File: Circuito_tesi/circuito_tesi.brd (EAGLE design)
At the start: 19 parts, among them IC1 317T, IC2 317T, IC3 317T, U1 NRF52832, U2 BME688

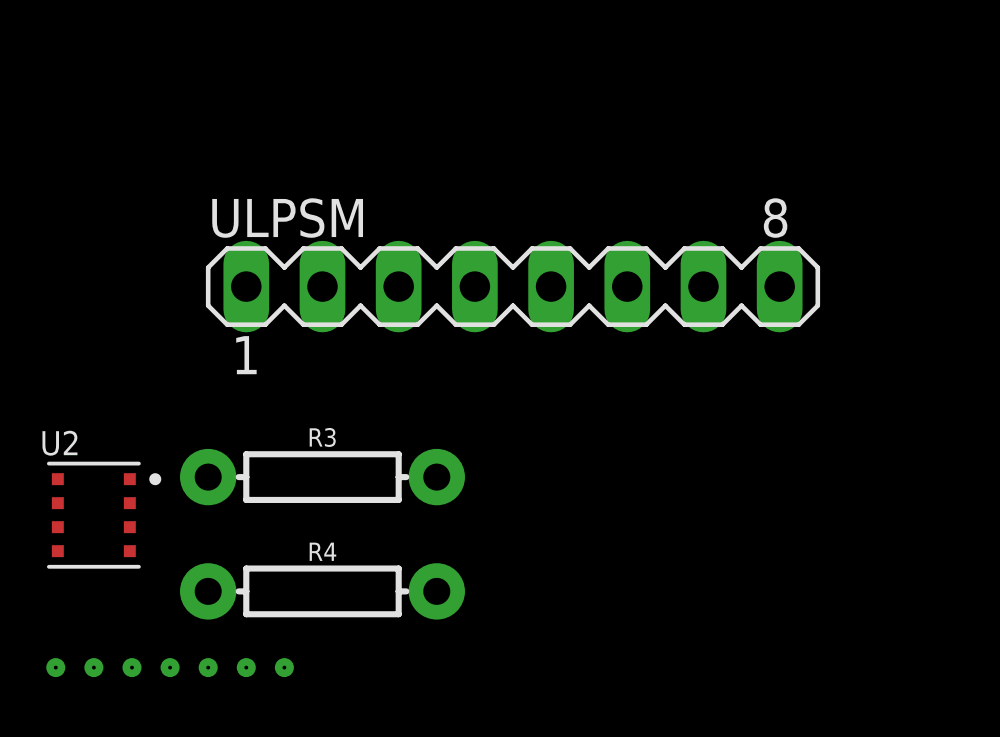
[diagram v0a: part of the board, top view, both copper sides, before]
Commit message: Attivato saadc
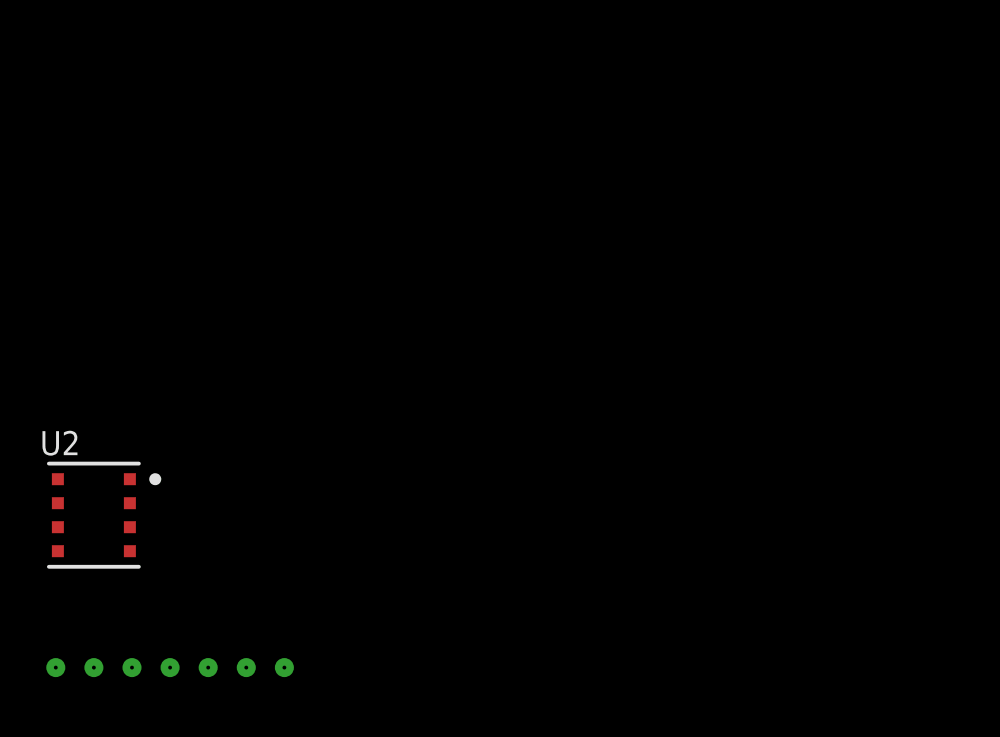
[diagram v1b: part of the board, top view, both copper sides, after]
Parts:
- removed R3, R4: 10k, SparkFun-Resistors:AXIAL-0.3
- removed ULPSM: (no value), con-lstb:MA08-1
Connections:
- removed net N$10: ULPSM.1
- removed net N$6: R3.P$2, R4.P$1, ULPSM.2
- net 3.3: no longer R3.P$1, R4.P$2, ULPSM.6, ULPSM.8
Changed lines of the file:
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@@
 <attribute name="VALUE" x="-93.98" y="-49.276" size="0.6096" layer="27" font="vector" ratio="20" align="top-center"/>
-</element>
-<element name="ULPSM" library="con-lstb" library_urn="urn:adsk.eagle:library:162" package="MA08-1" package3d_urn="urn:adsk.eagle:package:8343/1" value="" x="-87.63" y="-69.85" smashed="yes">
-<attribute name="MF" value="" x="-87.63" y="-69.85" size="1.778" layer="27" display="off"/>
-<attribute name="MPN" value="" x="-87.63" y="-69.85" size="1.778" layer="27" display="off"/>
-<attribute name="NAME" x="-97.79" y="-68.199" size="1.27" layer="25" ratio="10"/>
-<attribute name="OC_FARNELL" value="unknown" x="-87.63" y="-69.85" size="1.778" layer="27" display="off"/>
-<attribute name="OC_NEWARK" value="unknown" x="-87.63" y="-69.85" size="1.778" layer="27" display="off"/>
-<attribute name="POPULARITY" value="10" x="-87.63" y="-69.85" size="1.778" layer="27" display="off"/>
-<attribute name="VALUE" x="-88.9" y="-72.771" size="1.27" layer="27" ratio="10"/>
-</element>
-<element name="R3" library="SparkFun-Resistors" package="AXIAL-0.3" value="10k" x="-93.98" y="-76.2" smashed="yes">
-<attribute name="NAME" x="-93.98" y="-75.184" size="0.6096" layer="25" font="vector" ratio="20" align="bottom-center"/>
-<attribute name="PROD_ID" value="RES-08375" x="-93.98" y="-76.2" size="1.778" layer="27" display="off"/>
-<attribute name="VALUE" x="-93.98" y="-77.216" size="0.6096" layer="27" font="vector" ratio="20" align="top-center"/>
-</element>
-<element name="R4" library="SparkFun-Resistors" package="AXIAL-0.3" value="10k" x="-93.98" y="-80.01" smashed="yes">
-<attribute name="NAME" x="-93.98" y="-78.994" size="0.6096" layer="25" font="vector" ratio="20" align="bottom-center"/>
-<attribute name="PROD_ID" value="RES-08375" x="-93.98" y="-80.01" size="1.778" layer="27" display="off"/>
-<attribute name="VALUE" x="-93.98" y="-81.026" size="0.6096" layer="27" font="vector" ratio="20" align="top-center"/>
 </element>
 <element name="U2" library="BME688" package="IC_BME688" value="BME688" x="-101.6" y="-77.47" smashed="yes">
@@
 <contactref element="B1" pad="GND1"/>
 <contactref element="B1" pad="GND2"/>
-<contactref element="R4" pad="P$2"/>
-<contactref element="ULPSM" pad="6"/>
-<contactref element="ULPSM" pad="8"/>
-<contactref element="R3" pad="P$1"/>
 <contactref element="IC2" pad="2"/>
 <contactref element="C2" pad="1"/>
@@
 <wire x1="-102.8" y1="-76.27" x2="-102.8" y2="-77.87" width="0" layer="19" extent="1-1"/>
 <wire x1="-100.4" y1="-77.07" x2="-102.8" y2="-77.87" width="0" layer="19" extent="1-1"/>
-<wire x1="-97.79" y1="-76.2" x2="-100.4" y2="-77.07" width="0" layer="19" extent="1-1"/>
-<wire x1="-95.25" y1="-82.55" x2="-97.79" y2="-76.2" width="0" layer="19" extent="1-1"/>
-<wire x1="-90.17" y1="-80.01" x2="-95.25" y2="-82.55" width="0" layer="19" extent="1-1"/>
-<wire x1="-83.82" y1="-69.85" x2="-90.17" y2="-80.01" width="0" layer="19" extent="1-1"/>
-<wire x1="-78.74" y1="-69.85" x2="-83.82" y2="-69.85" width="0" layer="19" extent="1-1"/>
-<wire x1="-90.17" y1="-48.26" x2="-83.82" y2="-69.85" width="0" layer="19" extent="1-1"/>
+<wire x1="-95.25" y1="-82.55" x2="-100.4" y2="-77.07" width="0" layer="19" extent="1-1"/>
+<wire x1="-90.17" y1="-48.26" x2="-100.4" y2="-77.07" width="0" layer="19" extent="1-1"/>
 <wire x1="-90.17" y1="-44.45" x2="-90.17" y2="-48.26" width="0" layer="19" extent="1-1"/>
 <wire x1="-95.67" y1="-33.02" x2="-90.17" y2="-44.45" width="0" layer="19" extent="1-1"/>
@@
 <wire x1="-15.11" y1="-10.48" x2="-81.28" y2="-8.89" width="0" layer="19" extent="1-1"/>
 </signal>
-<signal name="N$6">
-<contactref element="R3" pad="P$2"/>
-<contactref element="ULPSM" pad="2"/>
-<contactref element="R4" pad="P$1"/>
-<wire x1="-90.17" y1="-76.2" x2="-97.79" y2="-80.01" width="0" layer="19" extent="1-1"/>
-<wire x1="-93.98" y1="-69.85" x2="-90.17" y2="-76.2" width="0" layer="19" extent="1-1"/>
-</signal>
-<signal name="N$10">
-<contactref element="ULPSM" pad="1"/>
-</signal>
 <signal name="N$8">

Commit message: Aggiunta lettura MICS6814
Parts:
- removed C3: 0.1uF, SparkFun-Capacitors:0603
- removed C4: 22uF, SparkFun-Capacitors:0805
- removed IC3: 317T, linear:TO220H
- added U3: MICS-6814, MICS-6814:SENSOR_MICS-6814
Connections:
- removed net N$2: C4.1, IC3.2
- net 3.3: no longer C3.2, C4.2, IC3.1
- net VCC-ISO: no longer C3.1, IC3.3
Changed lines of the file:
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@@
 <attribute name="VALUE" x="-37.084" y="-9.779" size="1.778" layer="27" ratio="10" rot="R90"/>
-</element>
-<element name="IC3" library="linear" library_urn="urn:adsk.eagle:library:262" package="TO220H" package3d_urn="urn:adsk.eagle:package:16414/1" value="317T" x="-60.96" y="1.27" smashed="yes">
-<attribute name="NAME" x="-66.421" y="-9.652" size="1.778" layer="25" ratio="10" rot="R90"/>
-<attribute name="POPULARITY" value="7" x="-60.96" y="1.27" size="1.778" layer="27" display="off"/>
-<attribute name="VALUE" x="-53.594" y="-9.779" size="1.778" layer="27" ratio="10" rot="R90"/>
 </element>
 <element name="B1" library="SparkFun-Boards" package="SPARKFUN_LOGIC_LEVEL_CONVERTER" value="SPARKFUN_LOGIC_LEVEL_CONVERTER" x="-76.2" y="-2.54" smashed="yes">
@@
 <attribute name="PROD_ID" value="CAP-11330" x="-96.52" y="-17.78" size="1.778" layer="27" display="off"/>
 <attribute name="VALUE" x="-96.52" y="-18.669" size="0.6096" layer="27" font="vector" ratio="20" align="top-center"/>
-</element>
-<element name="C3" library="SparkFun-Capacitors" package="0603" value="0.1uF" x="-96.52" y="-21.59" smashed="yes">
-<attribute name="NAME" x="-96.52" y="-20.828" size="0.6096" layer="25" font="vector" ratio="20" align="bottom-center"/>
-<attribute name="PROD_ID" value="CAP-08604" x="-96.52" y="-21.59" size="1.778" layer="27" display="off"/>
-<attribute name="VALUE" x="-96.52" y="-22.352" size="0.6096" layer="27" font="vector" ratio="20" align="top-center"/>
-</element>
-<element name="C4" library="SparkFun-Capacitors" package="0805" value="22uF" x="-96.52" y="-25.4" smashed="yes">
-<attribute name="NAME" x="-96.52" y="-24.511" size="0.6096" layer="25" font="vector" ratio="20" align="bottom-center"/>
-<attribute name="PROD_ID" value="CAP-08402" x="-96.52" y="-25.4" size="1.778" layer="27" display="off"/>
-<attribute name="VALUE" x="-96.52" y="-26.289" size="0.6096" layer="27" font="vector" ratio="20" align="top-center"/>
 </element>
 <element name="C5" library="SparkFun-Capacitors" package="0805" value="0.33µF" x="-96.52" y="-29.21" smashed="yes">
@@
 </element>
 <element name="SCD4X" library="SCD41-D-R1" package="SCD4X_SCD4X" value="SCD4XSCD4X_SCD4X_SCD4X" x="-102.87" y="-82.55" smashed="yes"/>
+<element name="U3" library="MICS-6814" package="SENSOR_MICS-6814" value="MICS-6814" x="-110.49" y="-76.2" smashed="yes">
+<attribute name="AVAILABILITY" value="Not in stock" x="-110.49" y="-76.2" size="1.778" layer="27" display="off"/>
+<attribute name="DESCRIPTION" value=" MiCS-6814 Air Quality Sensor mikroBUS™ Click™ Platform Evaluation Expansion Board " x="-110.49" y="-76.2" size="1.778" layer="27" display="off"/>
+<attribute name="MF" value="MikroElektronika" x="-110.49" y="-76.2" size="1.778" layer="27" display="off"/>
+<attribute name="MP" value="MICS-6814" x="-110.49" y="-76.2" size="1.778" layer="27" display="off"/>
+<attribute name="NAME" x="-114.3" y="-71.12" size="1.778" layer="25"/>
+<attribute name="PACKAGE" value="None" x="-110.49" y="-76.2" size="1.778" layer="27" display="off"/>
+<attribute name="PRICE" value="None" x="-110.49" y="-76.2" size="1.778" layer="27" display="off"/>
+<attribute name="VALUE" x="-114.3" y="-82.55" size="1.778" layer="27"/>
+</element>
 </elements>
 <signals>
@@
 <contactref element="IC1" pad="3"/>
 <contactref element="C5" pad="1"/>
-<contactref element="IC3" pad="3"/>
-<contactref element="C3" pad="1"/>
-<wire x1="-97.37" y1="-21.59" x2="-97.42" y2="-29.21" width="0" layer="19" extent="1-1"/>
-<wire x1="-97.42" y1="-13.97" x2="-97.37" y2="-21.59" width="0" layer="19" extent="1-1"/>
-<wire x1="-58.42" y1="-8.89" x2="-97.42" y2="-13.97" width="0" layer="19" extent="1-1"/>
-<wire x1="-41.91" y1="-8.89" x2="-58.42" y2="-8.89" width="0" layer="19" extent="1-1"/>
+<wire x1="-97.42" y1="-13.97" x2="-97.42" y2="-29.21" width="0" layer="19" extent="1-1"/>
+<wire x1="-41.91" y1="-8.89" x2="-97.42" y2="-13.97" width="0" layer="19" extent="1-1"/>
 <wire x1="-25.4" y1="-8.89" x2="-41.91" y2="-8.89" width="0" layer="19" extent="1-1"/>
 </signal>
 <signal name="3.3">
 <contactref element="IC2" pad="1"/>
-<contactref element="IC3" pad="1"/>
 <contactref element="IC1" pad="1"/>
 <contactref element="C1" pad="2"/>
@@
 <contactref element="C5" pad="2"/>
 <contactref element="C6" pad="2"/>
-<contactref element="C4" pad="2"/>
-<contactref element="C3" pad="2"/>
 <contactref element="B1" pad="GND1"/>
 <contactref element="B1" pad="GND2"/>
@@
 <wire x1="-95.67" y1="-33.02" x2="-90.17" y2="-44.45" width="0" layer="19" extent="1-1"/>
 <wire x1="-95.62" y1="-29.21" x2="-95.67" y2="-33.02" width="0" layer="19" extent="1-1"/>
-<wire x1="-95.62" y1="-25.4" x2="-95.62" y2="-29.21" width="0" layer="19" extent="1-1"/>
-<wire x1="-95.67" y1="-21.59" x2="-95.62" y2="-25.4" width="0" layer="19" extent="1-1"/>
-<wire x1="-95.62" y1="-17.78" x2="-95.67" y2="-21.59" width="0" layer="19" extent="1-1"/>
+<wire x1="-95.62" y1="-17.78" x2="-95.62" y2="-29.21" width="0" layer="19" extent="1-1"/>
 <wire x1="-97.42" y1="-17.78" x2="-95.62" y2="-17.78" width="0" layer="19" extent="1-1"/>
 <wire x1="-95.62" y1="-13.97" x2="-95.62" y2="-17.78" width="0" layer="19" extent="1-1"/>
@@
 <wire x1="-81.28" y1="-1.27" x2="-81.28" y2="-3.81" width="0" layer="19" extent="1-1"/>
 <wire x1="-71.12" y1="-3.81" x2="-81.28" y2="-3.81" width="0" layer="19" extent="1-1"/>
-<wire x1="-63.5" y1="-8.89" x2="-71.12" y2="-3.81" width="0" layer="19" extent="1-1"/>
-<wire x1="-46.99" y1="-8.89" x2="-63.5" y2="-8.89" width="0" layer="19" extent="1-1"/>
+<wire x1="-46.99" y1="-8.89" x2="-71.12" y2="-3.81" width="0" layer="19" extent="1-1"/>
 <wire x1="-44.45" y1="-8.89" x2="-46.99" y2="-8.89" width="0" layer="19" extent="1-1"/>
 <wire x1="-30.48" y1="-8.89" x2="-44.45" y2="-8.89" width="0" layer="19" extent="1-1"/>
@@
 <wire x1="-27.94" y1="-8.89" x2="-71.12" y2="-1.27" width="0" layer="19" extent="1-1"/>
 </signal>
-<signal name="N$2">
-<contactref element="IC3" pad="2"/>
-<contactref element="C4" pad="1"/>
-<wire x1="-60.96" y1="-8.89" x2="-97.42" y2="-25.4" width="0" layer="19" extent="1-1"/>
-</signal>
 <signal name="N$1">

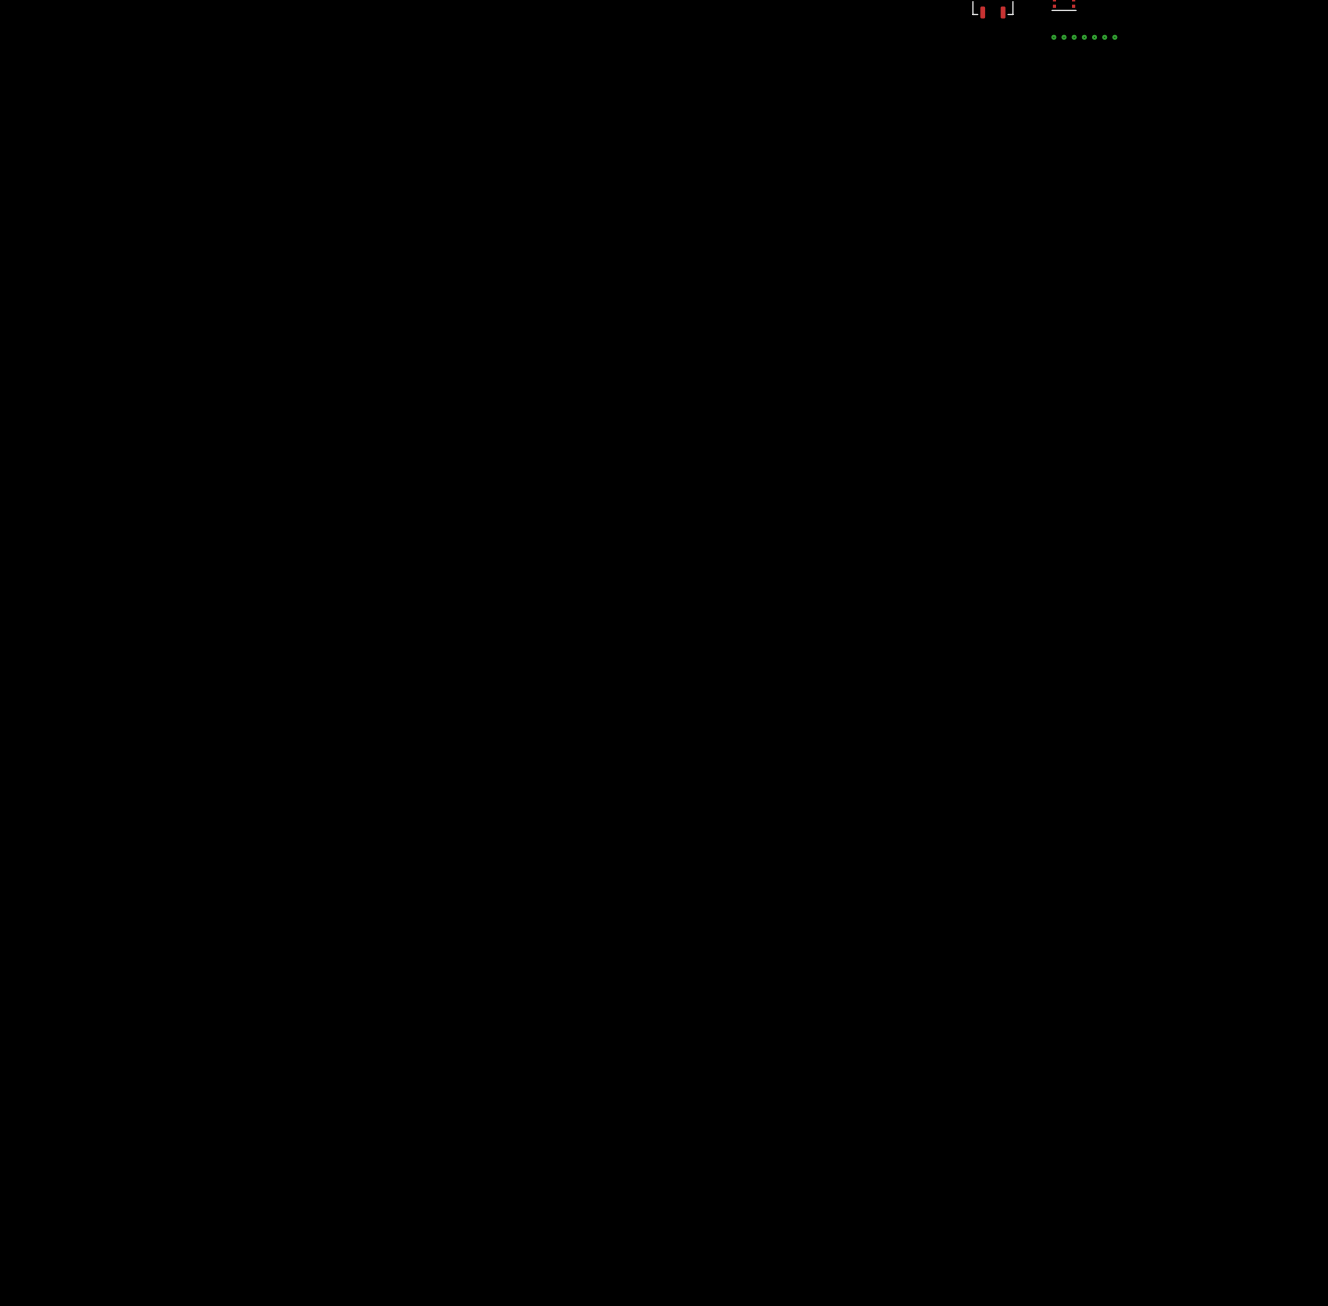
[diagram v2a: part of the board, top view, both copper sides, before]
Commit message: Completato schematico (resistenze non corrette)
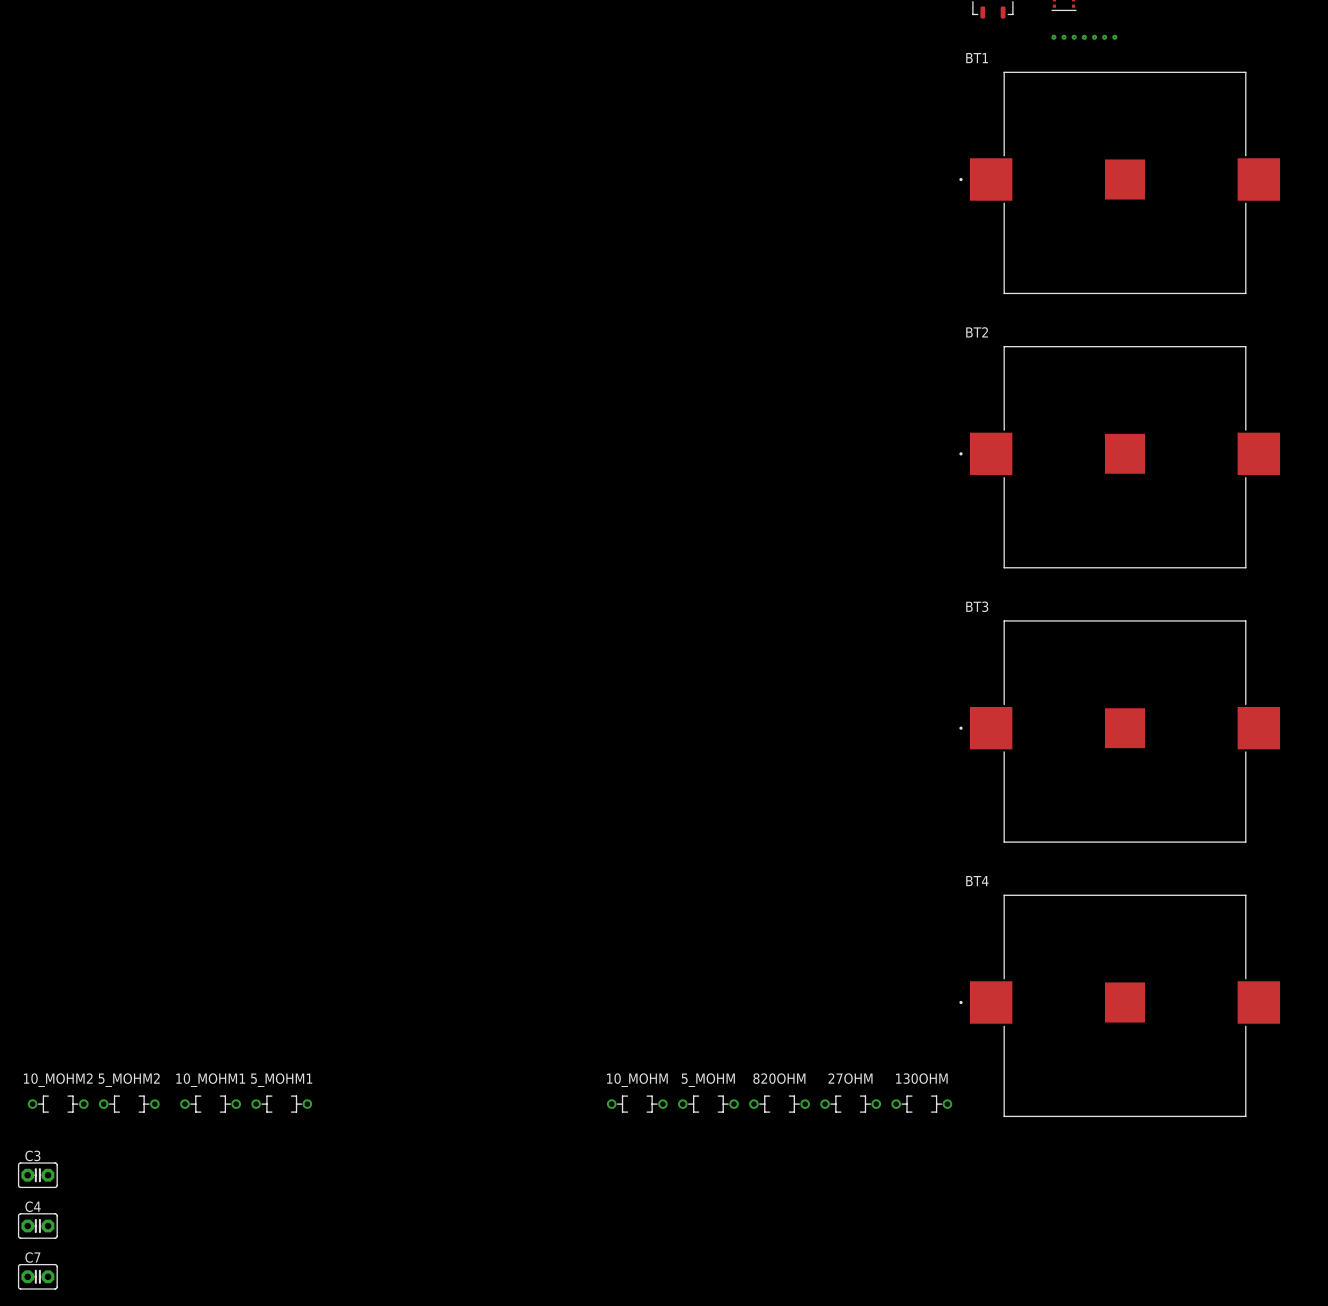
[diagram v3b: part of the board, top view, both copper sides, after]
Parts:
- added 10_MOHM, 10_MOHM1, 10_MOHM2, 130OHM, 27OHM, 5_MOHM, 5_MOHM1, 5_MOHM2, 820OHM: 1614992-1, 1614992-1:RESAD640W45L370D200
- added BT1, BT2, BT3, BT4: BHX1-2450-SM, BHX1-2450-SM:BAT_BHX1-2450-SM
- added C3, C4, C7: (no value), capacitor-wima:C2.5-3
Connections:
- removed net VCC-ISO: C1.1, C5.1, IC1.3, IC2.3
- new net N$10: U3.H
- new net N$11: 820OHM.1, U3.E, U3.G
- new net N$12: 27OHM.1, U3.C
- new net N$13: 130OHM.1, U3.K
- new net N$14: U3.D
- new net N$15: 5_MOHM.2
- new net N$16: 10_MOHM2.2, 5_MOHM2.1, C3.1, U1.6
- new net N$17: 10_MOHM.2, 5_MOHM.1, C7.1, U1.7
- new net N$18: 10_MOHM1.2, 5_MOHM1.1, C4.1, U1.5
- new net N$2: BT1.2, BT2.1, BT2.1_1
- new net N$4: BT2.2, BT3.1, BT3.1_1
- new net N$5: BT3.2, BT4.1, BT4.1_1
- new net N$6: U3.A
- new net N$9: BT1.1, BT1.1_1, C1.1, C5.1, IC1.3, IC2.3
- net 5V: now also 130OHM.2, 27OHM.2, 820OHM.2
- net GND: now also 10_MOHM.1, 10_MOHM1.1, 10_MOHM2.1, BT4.2, C3.2, C4.2, C7.2, U3.B, U3.F, U3.J
- net N$7: now also 5_MOHM1.2; no longer U1.6
- net N$8: now also 5_MOHM2.2; no longer U1.7
